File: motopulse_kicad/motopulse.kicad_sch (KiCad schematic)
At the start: 6 parts, among them J1 INMP441_Left, J2 INMP441_Right, J3 SSD1306_OLED, J4 Piezo_Sensor, U1 ESP32-S3-DevKitC-1-N16R8

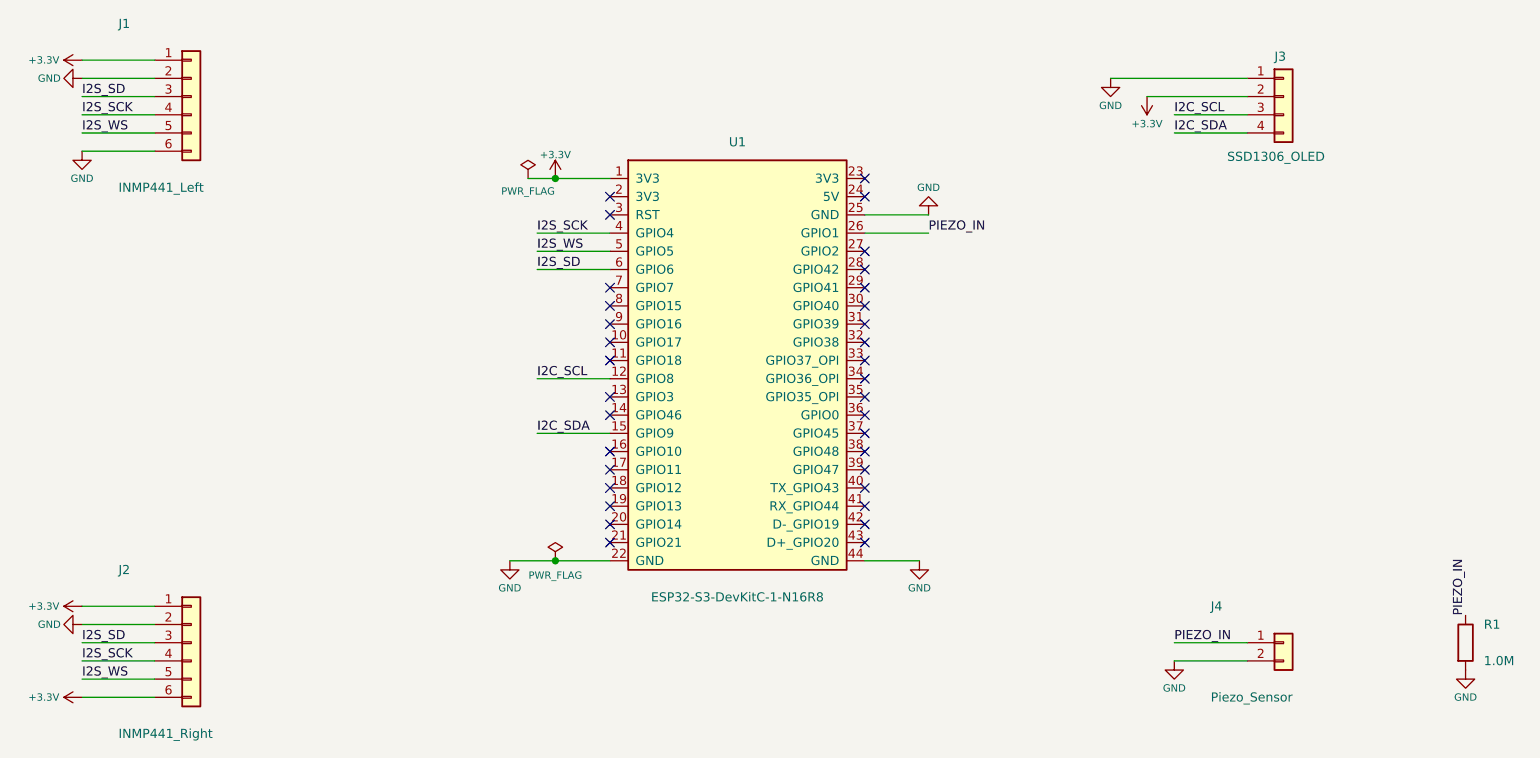
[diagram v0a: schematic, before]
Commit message: feat: implement autonomous continual self-learning engine and live telemetry dashboard
- Deploy embedded C++ Online Continual Learning Engine (ESP32OnlineVehicleLearner) with Welford streaming EMA adaptation
- Implement engine running verification gating via Piezo (GPIO 1) + I2S acoustic energy
- Add Anomaly Drift Guard freezing baseline updates during acoustic/vibration defects (>3.2 sigma)
- Add NVS Flash persistence saving vehicle profile across ignition cycles
- Add Arduino firmware sketch (firmware/motopulse_online_learner.ino) with FreeRTOS task on Core 1
- Integrate real-time continual learner telemetry into dashboard/server.py and web UI
- Add live self-learning status, operational regimes, Z-meter, and interactive demo controls in Cockpit UI
- Preserve user edits in KiCad carrier board schematic and PCB

Co-authored-by: ishannvn <ishannvn@users.noreply.github.com>
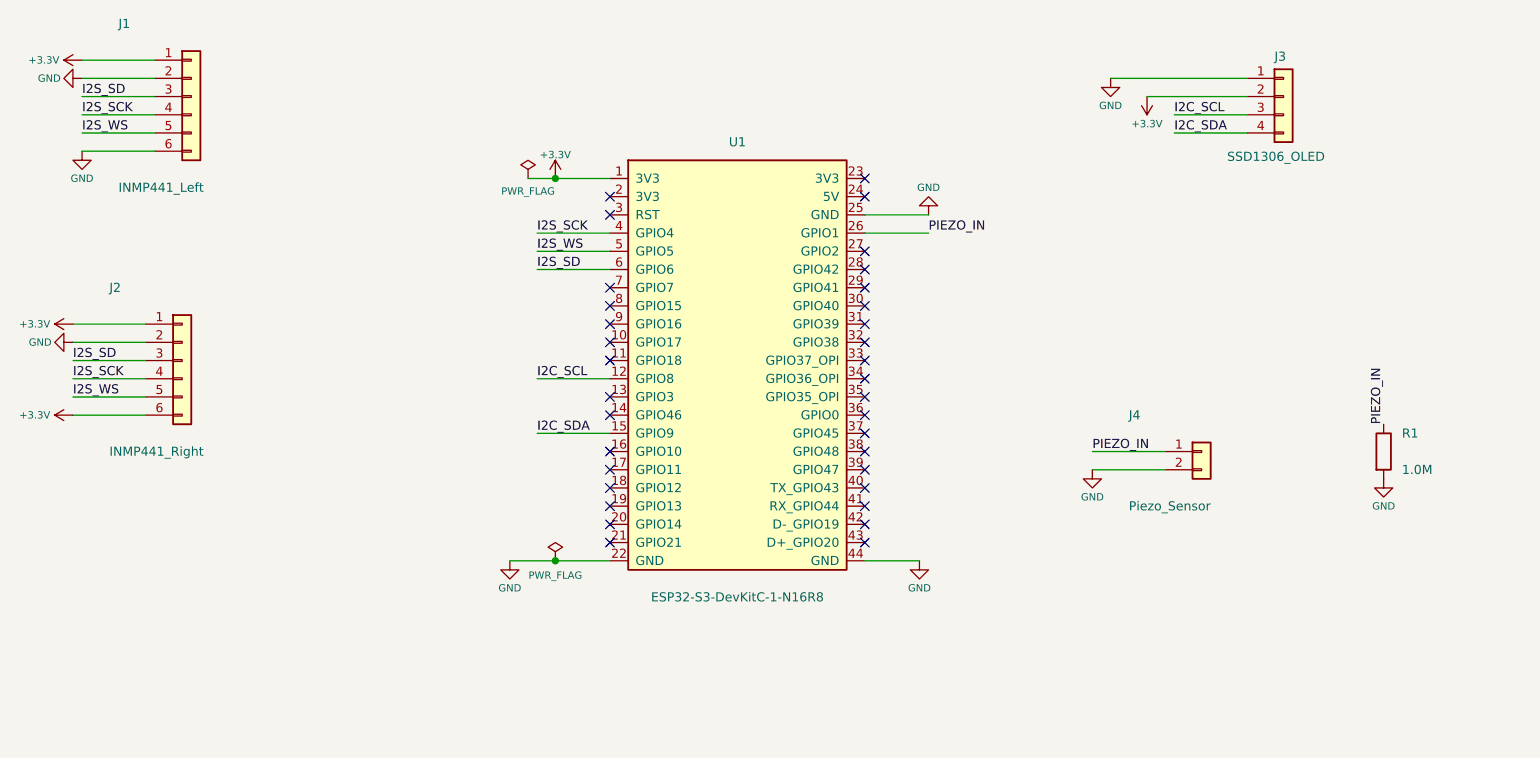
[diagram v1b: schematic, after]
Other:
- moved on the sheet: J2, J4, R1
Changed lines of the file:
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@@
 	(wire
 		(pts
-			(xy 58.42 157.48) (xy 48.26 157.48)
+			(xy 57.15 118.11) (xy 46.99 118.11)
 		)
 		(stroke
@@
 	(wire
 		(pts
-			(xy 210.82 152.4) (xy 200.66 152.4)
-		)
-		(stroke
-			(width 0)
-			(type default)
-		)
-	)
-	(wire
-		(pts
-			(xy 58.42 152.4) (xy 48.26 152.4)
-		)
-		(stroke
-			(width 0)
-			(type default)
-		)
-	)
-	(wire
-		(pts
-			(xy 58.42 160.02) (xy 48.26 160.02)
+			(xy 199.39 125.73) (xy 189.23 125.73)
+		)
+		(stroke
+			(width 0)
+			(type default)
+		)
+	)
+	(wire
+		(pts
+			(xy 57.15 113.03) (xy 46.99 113.03)
+		)
+		(stroke
+			(width 0)
+			(type default)
+		)
+	)
+	(wire
+		(pts
+			(xy 57.15 120.65) (xy 46.99 120.65)
 		)
 		(stroke
@@
 	(wire
 		(pts
-			(xy 210.82 154.94) (xy 200.66 154.94)
+			(xy 199.39 128.27) (xy 189.23 128.27)
 		)
 		(stroke
@@
 	(wire
 		(pts
-			(xy 58.42 154.94) (xy 48.26 154.94)
+			(xy 57.15 115.57) (xy 46.99 115.57)
 		)
 		(stroke
@@
 	(wire
 		(pts
-			(xy 58.42 149.86) (xy 48.26 149.86)
+			(xy 57.15 110.49) (xy 46.99 110.49)
 		)
 		(stroke
@@
 	(wire
 		(pts
-			(xy 58.42 147.32) (xy 48.26 147.32)
+			(xy 57.15 107.95) (xy 46.99 107.95)
 		)
 		(stroke
@@
 	)
 	(label "I2S_SD"
-		(at 48.26 152.4 0)
+		(at 46.99 113.03 0)
 		(effects
 			(font
@@
 	)
 	(label "PIEZO_IN"
-		(at 200.66 152.4 0)
+		(at 189.23 125.73 0)
 		(effects
 			(font
@@
 	)
 	(label "I2S_WS"
-		(at 48.26 157.48 0)
+		(at 46.99 118.11 0)
 		(effects
 			(font
@@
 	)
 	(label "PIEZO_IN"
-		(at 241.3 148.59 90)
+		(at 229.87 121.92 90)
 		(effects
 			(font
@@
 	)
 	(label "I2S_SCK"
-		(at 48.26 154.94 0)
+		(at 46.99 115.57 0)
 		(effects
 			(font
@@
 	(symbol
 		(lib_id "Connector_Generic:Conn_01x02")
-		(at 215.9 152.4 0)
+		(at 204.47 125.73 0)
 		(unit 1)
 		(body_style 1)
@@
 		(dnp no)
 		(property "Reference" "J4"
-			(at 205.74 147.32 0)
+			(at 194.31 120.65 0)
 			(show_name no)
 			(do_not_autoplace no)
@@
 		)
 		(property "Value" "Piezo_Sensor"
-			(at 205.74 160.02 0)
+			(at 194.31 133.35 0)
 			(show_name no)
 			(do_not_autoplace no)
@@
 		)
 		(property "Footprint" "Connector_PinHeader_2.54mm:PinHeader_1x02_P2.54mm_Vertical"
-			(at 215.9 152.4 0)
+			(at 204.47 125.73 0)
 			(hide yes)
 			(show_name no)
@@
 		)
 		(property "Datasheet" ""
-			(at 215.9 152.4 0)
+			(at 204.47 125.73 0)
 			(show_name no)
 			(do_not_autoplace no)
@@
 		)
 		(property "Description" ""
-			(at 215.9 152.4 0)
+			(at 204.47 125.73 0)
 			(show_name no)
 			(do_not_autoplace no)
@@
 	(symbol
 		(lib_id "power:+3.3V")
-		(at 48.26 147.32 90)
+		(at 46.99 107.95 90)
 		(unit 1)
 		(body_style 1)
@@
 		(dnp no)
 		(property "Reference" "#PWR08"
-			(at 48.26 147.32 0)
+			(at 46.99 107.95 0)
 			(hide yes)
 			(show_name no)
@@
 		)
 		(property "Value" "+3.3V"
-			(at 42.926 147.32 90)
+			(at 41.656 107.95 90)
 			(show_name no)
 			(do_not_autoplace no)
@@
 		)
 		(property "Footprint" ""
-			(at 48.26 147.32 0)
+			(at 46.99 107.95 0)
 			(hide yes)
 			(show_name no)
@@
 		)
 		(property "Datasheet" ""
-			(at 48.26 147.32 0)
+			(at 46.99 107.95 0)
 			(show_name no)
 			(do_not_autoplace no)
@@
 		)
 		(property "Description" ""
-			(at 48.26 147.32 0)
+			(at 46.99 107.95 0)
 			(show_name no)
 			(do_not_autoplace no)
@@
 	(symbol
 		(lib_id "power:+3.3V")
-		(at 48.26 160.02 90)
+		(at 46.99 120.65 90)
 		(unit 1)
 		(body_style 1)
@@
 		(dnp no)
 		(property "Reference" "#PWR10"
-			(at 48.26 160.02 0)
+			(at 46.99 120.65 0)
 			(hide yes)
 			(show_name no)
@@
 		)
 		(property "Value" "+3.3V"
-			(at 42.926 160.02 90)
+			(at 41.656 120.65 90)
 			(show_name no)
 			(do_not_autoplace no)
@@
 		)
 		(property "Footprint" ""
-			(at 48.26 160.02 0)
+			(at 46.99 120.65 0)
 			(hide yes)
 			(show_name no)
@@
 		)
 		(property "Datasheet" ""
-			(at 48.26 160.02 0)
+			(at 46.99 120.65 0)
 			(show_name no)
 			(do_not_autoplace no)
@@
 		)
 		(property "Description" ""
-			(at 48.26 160.02 0)
+			(at 46.99 120.65 0)
 			(show_name no)
 			(do_not_autoplace no)
@@
 	(symbol
 		(lib_id "power:GND")
-		(at 200.66 154.94 0)
+		(at 189.23 128.27 0)
 		(unit 1)
 		(body_style 1)
@@
 		(dnp no)
 		(property "Reference" "#PWR13"
-			(at 200.66 154.94 0)
+			(at 189.23 128.27 0)
 			(hide yes)
 			(show_name no)
@@
 		)
 		(property "Value" "GND"
-			(at 200.66 158.75 0)
+			(at 189.23 132.08 0)
 			(show_name no)
 			(do_not_autoplace no)
@@
 		)
 		(property "Footprint" ""
-			(at 200.66 154.94 0)
+			(at 189.23 128.27 0)
 			(hide yes)
 			(show_name no)
@@
 		)
 		(property "Datasheet" ""
-			(at 200.66 154.94 0)
+			(at 189.23 128.27 0)
 			(show_name no)
 			(do_not_autoplace no)
@@
 		)
 		(property "Description" ""
-			(at 200.66 154.94 0)
+			(at 189.23 128.27 0)
 			(show_name no)
 			(do_not_autoplace no)
@@
 	(symbol
 		(lib_id "Connector_Generic:Conn_01x06")
-		(at 63.5 152.4 0)
+		(at 62.23 113.03 0)
 		(unit 1)
 		(body_style 1)
@@
 		(dnp no)
 		(property "Reference" "J2"
-			(at 53.34 142.24 0)
+			(at 52.07 102.87 0)
 			(show_name no)
 			(do_not_autoplace no)
@@
 		)
 		(property "Value" "INMP441_Right"
-			(at 53.34 165.1 0)
+			(at 52.07 125.73 0)
 			(show_name no)
 			(do_not_autoplace no)
@@
 		)
 		(property "Footprint" "Connector_PinHeader_2.54mm:PinHeader_1x06_P2.54mm_Vertical"
-			(at 63.5 152.4 0)
+			(at 62.23 113.03 0)
 			(hide yes)
 			(show_name no)
@@
 		)
 		(property "Datasheet" ""
-			(at 63.5 152.4 0)
+			(at 62.23 113.03 0)
 			(show_name no)
 			(do_not_autoplace no)
@@
 		)
 		(property "Description" ""
-			(at 63.5 152.4 0)
+			(at 62.23 113.03 0)
 			(show_name no)
 			(do_not_autoplace no)
@@
 	(symbol
 		(lib_id "Device:R")
-		(at 241.3 152.4 0)
+		(at 229.87 125.73 0)
 		(unit 1)
 		(body_style 1)
@@
 		(dnp no)
 		(property "Reference" "R1"
-			(at 243.84 149.86 0)
+			(at 232.41 123.19 0)
 			(show_name no)
 			(do_not_autoplace no)
@@
 		)
 		(property "Value" "1.0M"
-			(at 243.84 154.94 0)
+			(at 232.41 128.27 0)
 			(show_name no)
 			(do_not_autoplace no)
@@
 		)
 		(property "Footprint" "Resistor_SMD:R_0805_2012Metric"
-			(at 241.3 152.4 0)
+			(at 229.87 125.73 0)
 			(hide yes)
 			(show_name no)
@@
 		)
 		(property "Datasheet" ""
-			(at 241.3 152.4 0)
+			(at 229.87 125.73 0)
 			(show_name no)
 			(do_not_autoplace no)
@@
 		)
 		(property "Description" ""
-			(at 241.3 152.4 0)
+			(at 229.87 125.73 0)
 			(show_name no)
 			(do_not_autoplace no)
@@
 	(symbol
 		(lib_id "power:GND")
-		(at 48.26 149.86 270)
+		(at 46.99 110.49 270)
 		(unit 1)
 		(body_style 1)
@@
 		(dnp no)
 		(property "Reference" "#PWR09"
-			(at 48.26 149.86 0)
+			(at 46.99 110.49 0)
 			(hide yes)
 			(show_name no)
@@
 		)
 		(property "Value" "GND"
-			(at 43.688 149.86 90)
+			(at 42.418 110.49 90)
 			(show_name no)
 			(do_not_autoplace no)
@@
 		)
 		(property "Footprint" ""
-			(at 48.26 149.86 0)
+			(at 46.99 110.49 0)
 			(hide yes)
 			(show_name no)
@@
 		)
 		(property "Datasheet" ""
-			(at 48.26 149.86 0)
+			(at 46.99 110.49 0)
 			(show_name no)
 			(do_not_autoplace no)
@@
 		)
 		(property "Description" ""
-			(at 48.26 149.86 0)
+			(at 46.99 110.49 0)
 			(show_name no)
 			(do_not_autoplace no)
@@
 	(symbol
 		(lib_id "power:GND")
-		(at 241.3 156.21 0)
+		(at 229.87 129.54 0)
 		(unit 1)
 		(body_style 1)
@@
 		(dnp no)
 		(property "Reference" "#PWR14"
-			(at 241.3 156.21 0)
+			(at 229.87 129.54 0)
 			(hide yes)
 			(show_name no)
@@
 		)
 		(property "Value" "GND"
-			(at 241.3 160.02 0)
+			(at 229.87 133.35 0)
 			(show_name no)
 			(do_not_autoplace no)
@@
 		)
 		(property "Footprint" ""
-			(at 241.3 156.21 0)
+			(at 229.87 129.54 0)
 			(hide yes)
 			(show_name no)
@@
 		)
 		(property "Datasheet" ""
-			(at 241.3 156.21 0)
+			(at 229.87 129.54 0)
 			(show_name no)
 			(do_not_autoplace no)
@@
 		)
 		(property "Description" ""
-			(at 241.3 156.21 0)
-			(show_name no)
-			(do_not_autoplace no)
+			(at 229.87 129.54 0)
+			(show_name no)
+			(do_not_autoplace no)
